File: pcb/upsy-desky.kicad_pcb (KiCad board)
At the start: 2 copper layers, 40.9 x 58 mm, 48 parts, among them J1 RJ45, J2 RJ45, J3 USB_C_ReceptacleUSB2.0, Q1 MMBT3904, Q2 MMBT3904, Q3 BSS138, Q4 BSS138, Q5 BSS138, Q6 BSS138, Q7 BSS138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

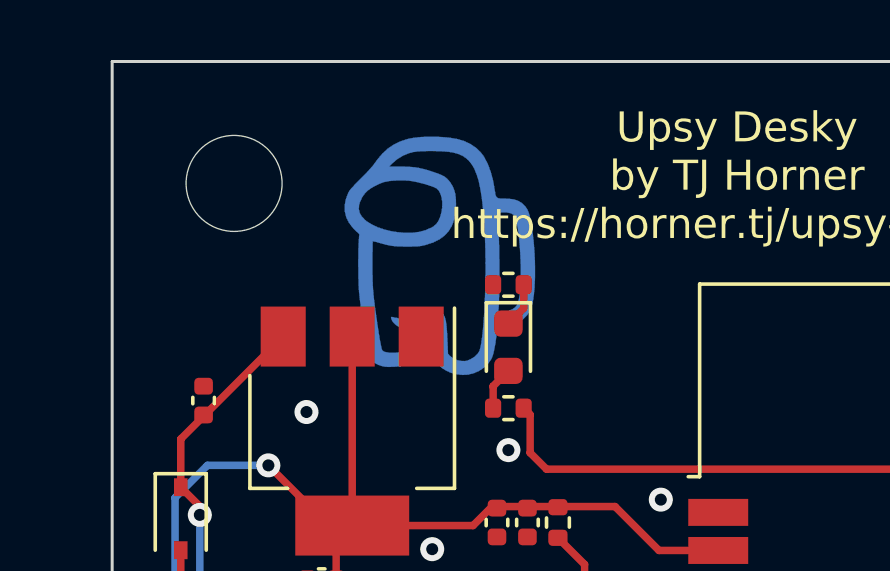
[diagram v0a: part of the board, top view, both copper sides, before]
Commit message: pcb: Update RJ45 part number
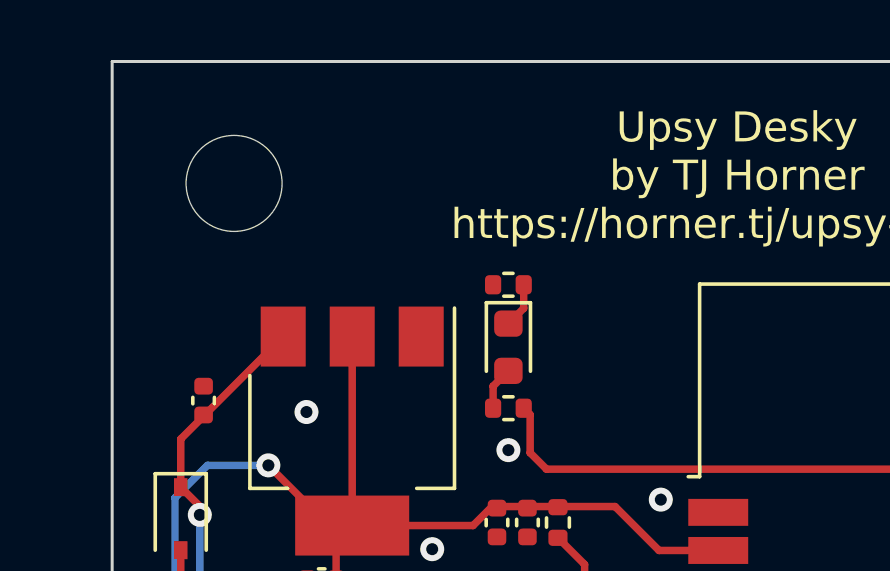
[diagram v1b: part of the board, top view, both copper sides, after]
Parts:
- removed Ref**: Val**, footprints:amongy

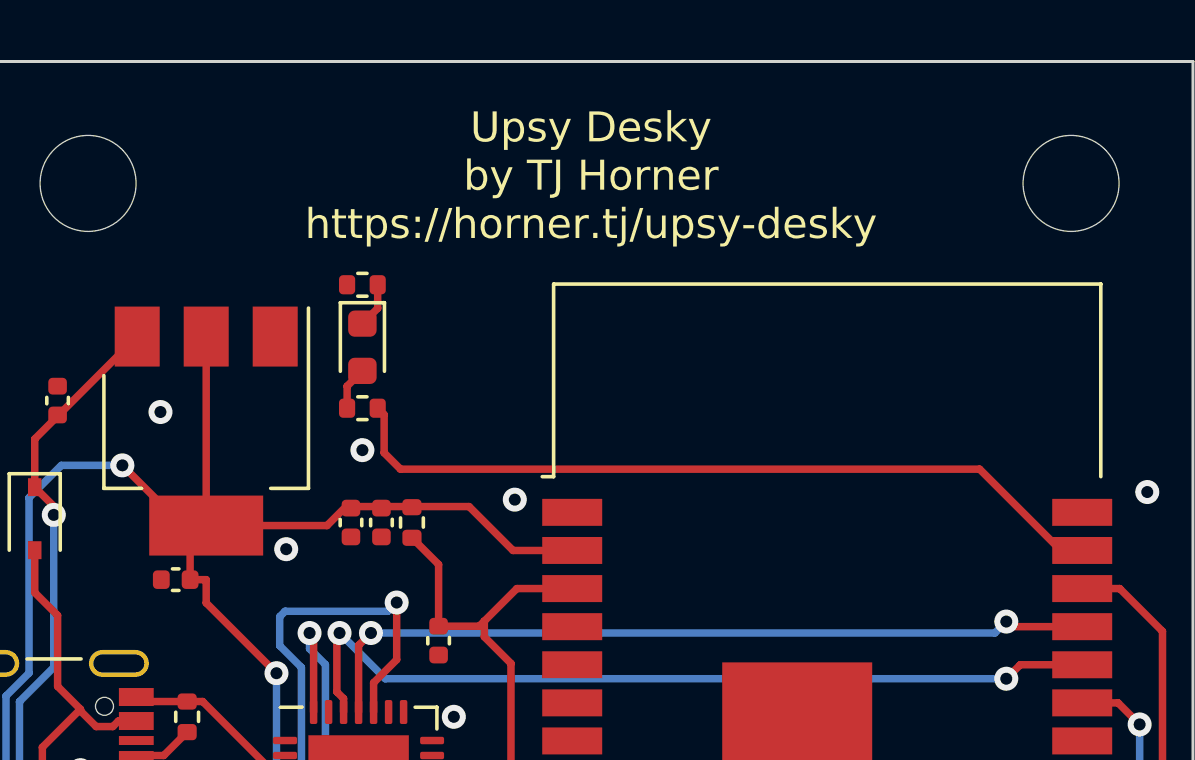
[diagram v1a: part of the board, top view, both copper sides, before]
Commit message: pcb: slight revision with logo on silkscreen
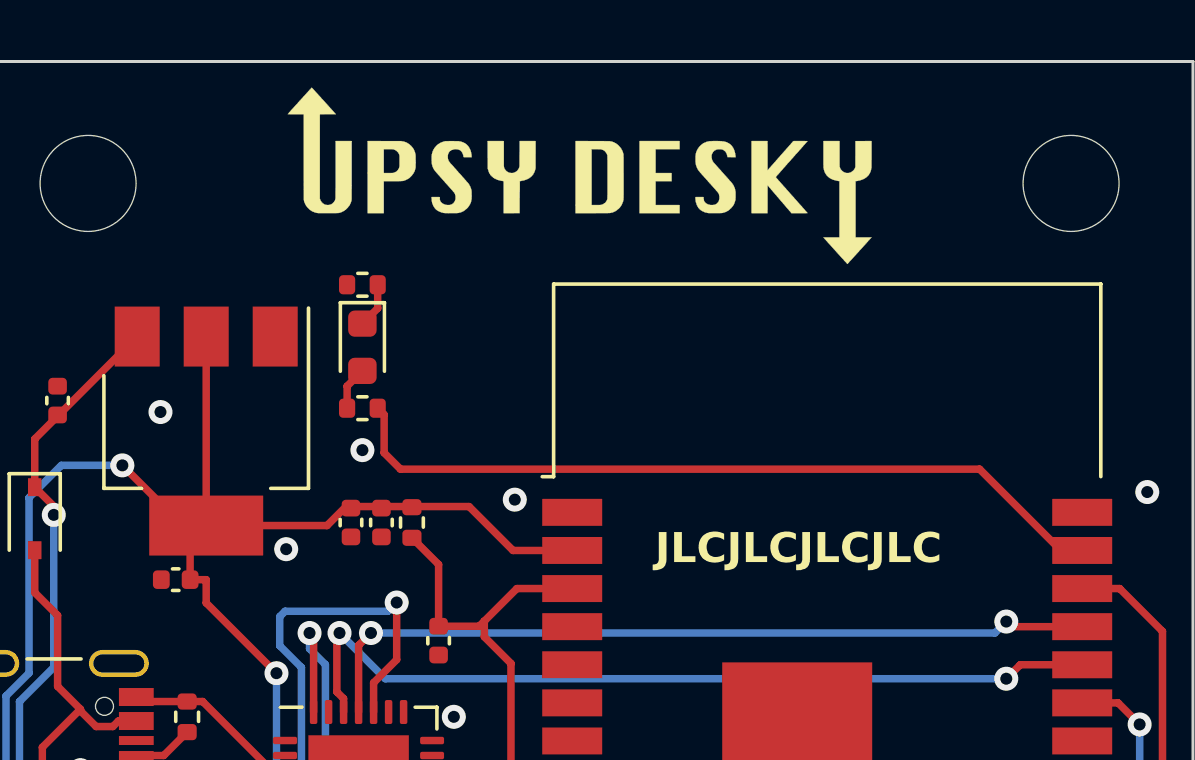
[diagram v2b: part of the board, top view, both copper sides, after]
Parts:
- added Ref**: Val**, footprints:dark_logotype_horizontal, F.Cu at (146.7, 74.8)
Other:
- board text added: "JLCJLCJLCJLC"
- board text removed: "Upsy Desky by TJ Horner https://horner.tj/upsy-desky"
